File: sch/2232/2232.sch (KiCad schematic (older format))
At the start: 57 parts

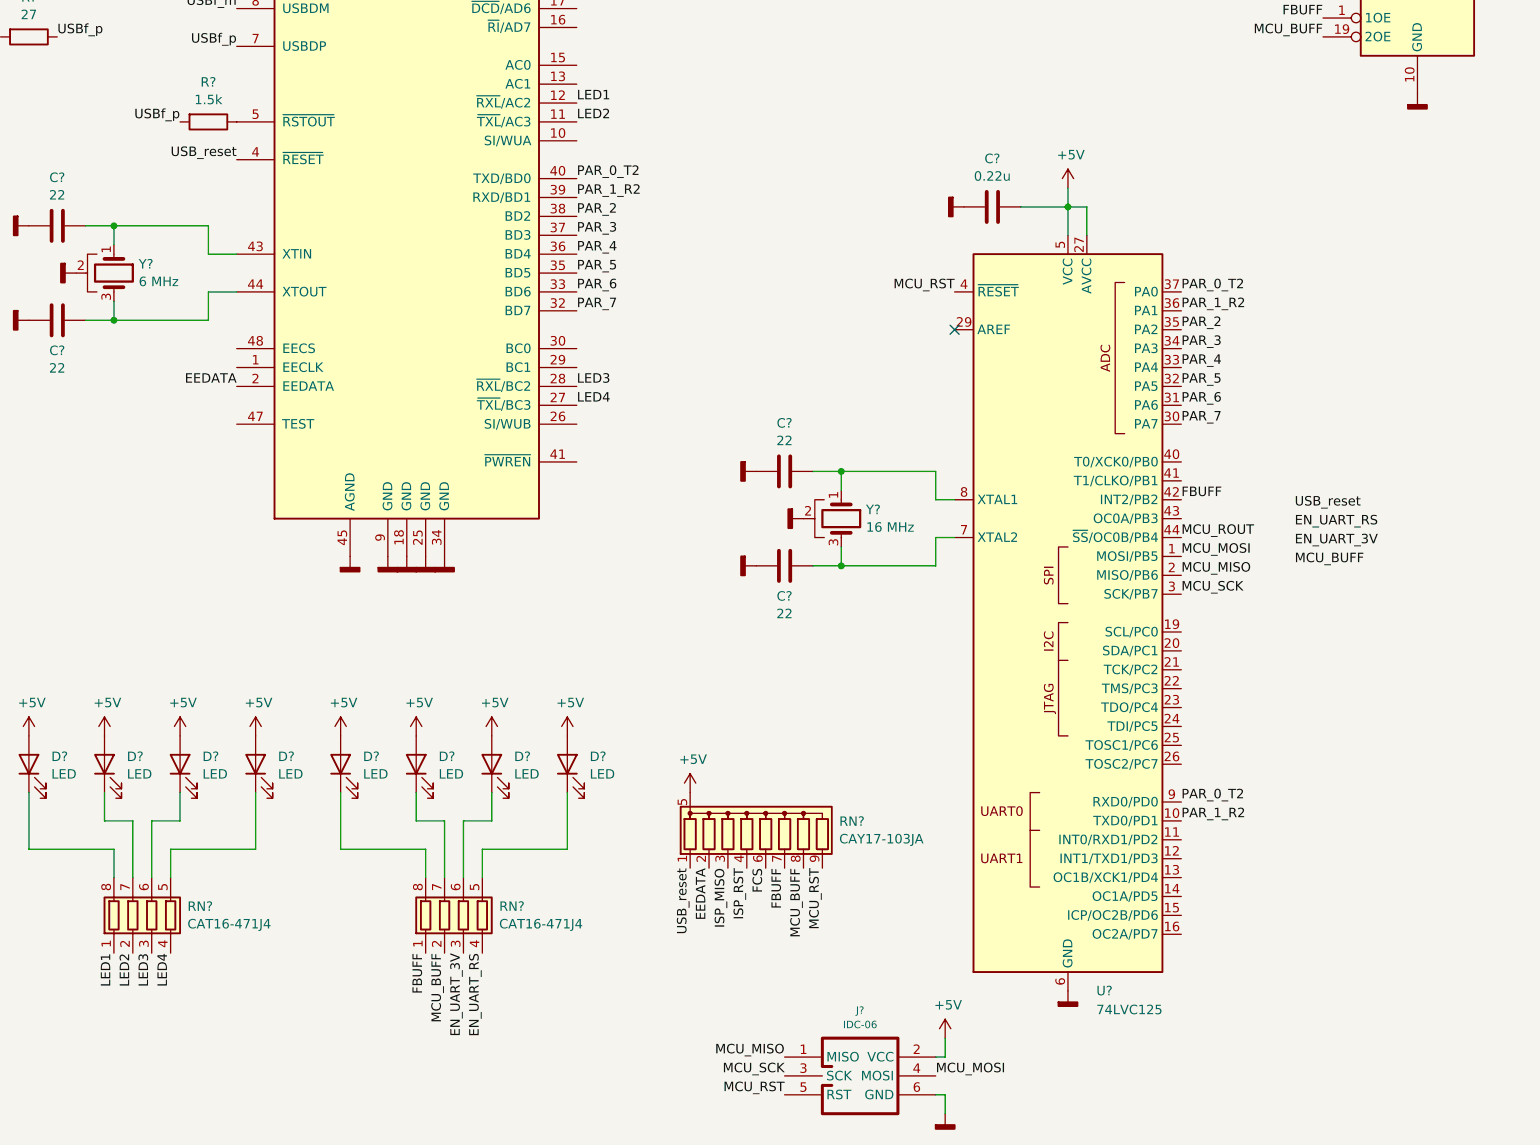
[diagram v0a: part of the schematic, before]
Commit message: Strobes added
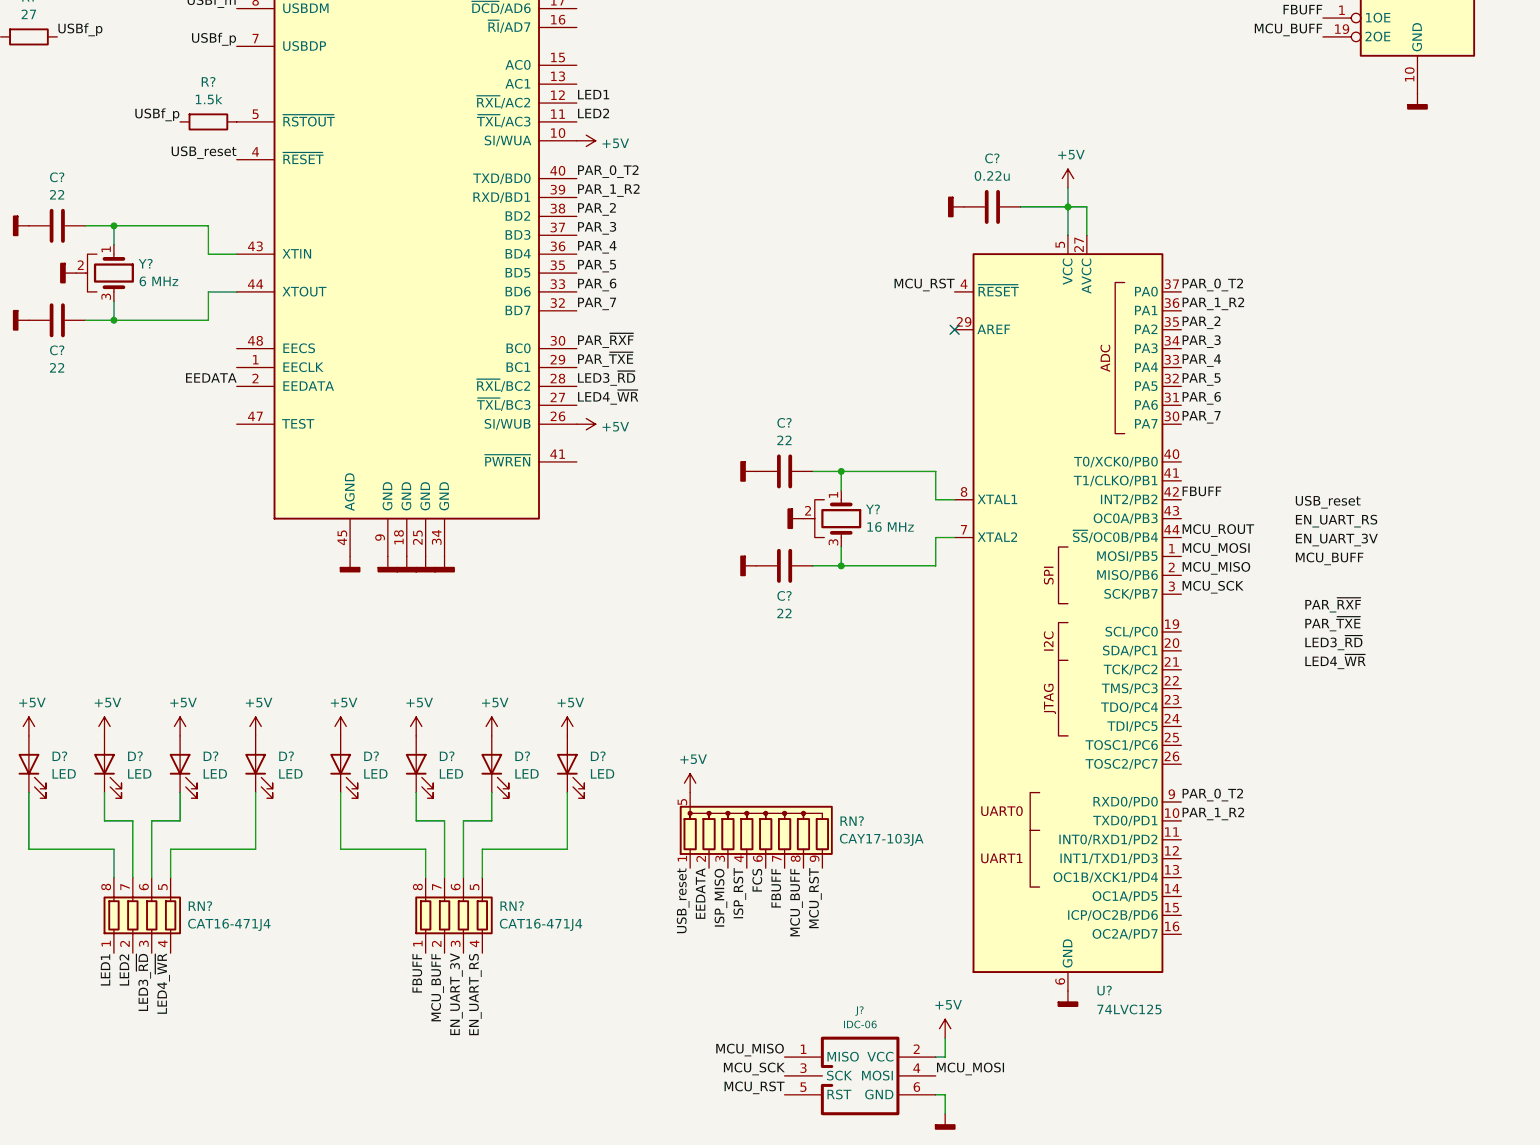
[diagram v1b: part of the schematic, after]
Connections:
- net +5V: now also U?.10 (SI/WUA), U?.26 (SI/WUB)
- net PAR_~TXE: now reaches U?.29 (BC1)
- net PAR_~RXF: now reaches U?.30 (BC0)
- net LED3 renamed LED3_~RD
- net LED4 renamed LED4_~WR
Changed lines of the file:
@@
 LED1
 Text Label 4300 6650 0    50   ~ 0
-LED3
+LED3_~RD
 $Comp
 L Device:Crystal_GND2 Y?
@@
 Text Label 4300 5250 0    50   ~ 0
 LED2
-Text Label 2050 9650 3    50   ~ 0
-LED3
 Text Label 4300 6750 0    50   ~ 0
-LED4
-Text Label 2150 9650 3    50   ~ 0
-LED4
+LED4_~WR
 $Comp
 L Device:LED D?
@@
 Text Label 3500 9650 3    50   ~ 0
 FBUFF
+Text Label 4300 6450 0    50   ~ 0
+PAR_~RXF
+Text Label 4300 6550 0    50   ~ 0
+PAR_~TXE
+$Comp
+L power:+5V #PWR?
+U 1 1 5FD4B651
+P 4300 6850
+F 0 "#PWR?" H 4300 6700 50  0001 C CNN
+F 1 "+5V" V 4315 6979 50  0000 L CNN
+F 2 "" H 4300 6850 50  0001 C CNN
+F 3 "" H 4300 6850 50  0001 C CNN
+	1    4300 6850
+	0    1    1    0
+$EndComp
+$Comp
+L power:+5V #PWR?
+U 1 1 5FD4BEFE
+P 4300 5350
+F 0 "#PWR?" H 4300 5200 50  0001 C CNN
+F 1 "+5V" V 4315 5479 50  0000 L CNN
+F 2 "" H 4300 5350 50  0001 C CNN
+F 3 "" H 4300 5350 50  0001 C CNN
+	1    4300 5350
+	0    1    1    0
+$EndComp
+Text Label 2050 9650 3    50   ~ 0
+LED3_~RD
+Text Label 2150 9650 3    50   ~ 0
+LED4_~WR
+Text Label 8150 8050 0    50   ~ 0
+LED3_~RD
+Text Label 8150 8150 0    50   ~ 0
+LED4_~WR
+Text Label 8150 7850 0    50   ~ 0
+PAR_~RXF
+Text Label 8150 7950 0    50   ~ 0
+PAR_~TXE
 $EndSCHEMATC

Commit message: HC138 added
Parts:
- added U?: 74HC138, NevaDA:SOIC-16, symbol symbol:74HC138
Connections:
- net +5V: now also U?.16 (VCC)
- net GNDD: now also U?.47 (TEST), U?.8 (GND)
- no-connect marks 3 -> 5
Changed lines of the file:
@@
 Text Label 10450 2050 3    50   ~ 0
 RX2_3V
-Text Label 8100 7500 0    50   ~ 0
+Text Label 12000 6350 0    50   ~ 0
 EN_UART_3V
-Text Label 8100 7400 0    50   ~ 0
+Text Label 12000 6250 0    50   ~ 0
 EN_UART_RS
 Text Label 4300 4250 0    50   ~ 0
@@
 Text Label 8150 7950 0    50   ~ 0
 PAR_~TXE
+$Comp
+L power:GNDD #PWR?
+U 1 1 5FD5E900
+P 2500 6850
+F 0 "#PWR?" H 2500 6600 50  0001 C CNN
+F 1 "GNDD" V 2504 6740 50  0001 R CNN
+F 2 "" H 2500 6850 50  0001 C CNN
+F 3 "" H 2500 6850 50  0001 C CNN
+	1    2500 6850
+	1    0    0    -1
+$EndComp
+NoConn ~ 2500 6550
+NoConn ~ 2500 6450
+$Comp
+L symbol:74HC138 U?
+U 1 1 5FD71BB5
+P 11100 6000
+F 0 "U?" H 11400 6650 50  0000 C CNN
+F 1 "74HC138" H 11400 6550 50  0000 C CNN
+F 2 "NevaDA:SOIC-16" H 11100 6000 50  0001 C CNN
+F 3 "" H 11100 6000 50  0001 C CNN
+	1    11100 6000
+	1    0    0    -1
+$EndComp
+$Comp
+L power:+5V #PWR?
+U 1 1 5FD71FD2
+P 11100 5400
+F 0 "#PWR?" H 11100 5250 50  0001 C CNN
+F 1 "+5V" H 11115 5575 50  0000 C CNN
+F 2 "" H 11100 5400 50  0001 C CNN
+F 3 "" H 11100 5400 50  0001 C CNN
+	1    11100 5400
+	1    0    0    -1
+$EndComp
+$Comp
+L power:GNDD #PWR?
+U 1 1 5FD72DAF
+P 11100 6700
+F 0 "#PWR?" H 11100 6450 50  0001 C CNN
+F 1 "GNDD" V 11104 6590 50  0001 R CNN
+F 2 "" H 11100 6700 50  0001 C CNN
+F 3 "" H 11100 6700 50  0001 C CNN
+	1    11100 6700
+	1    0    0    -1
+$EndComp
 $EndSCHEMATC
